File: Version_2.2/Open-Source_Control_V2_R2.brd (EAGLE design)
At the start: 121.9 x 129.5 mm, 344 parts, among them IC10 MCP6002SMT, IC11 MCP6002SMT, IC12 MCP6002SMT, IC14 MCP6002SMT, IC2 ULN2003AD, IC4 74HC165D, IC5 74HC165D, J24 6p-2.54, K1 JS1-24V-F, K2 JS1-24V-F, K3 JS1-24V-F, K4 JS1-24V-F, K5 JS1-24V-F, Q1 MMBT2907, T4 DA2304-AL, U1 OSD3358-512M-ICB, U16 AT97SC3205T-G3M4400B, U2 TPD4S012_DRY_6_P1_M, U27 LAN8710, U28 TCAN1051HV, U29 MAX3483EESA+T, U4 APX811-31UGSOT, U40 ISO3086TDW, U5 TLVH431, U6 SN74LVC2G241_DCU_8, X1 10118194-0001LF, X10 MC4, X11 MC4, X12 MC4, X2 J0011D01BNL, X21 MC10, X24 MSTBA2, X3 MC4, X4 CTI-JTAG, X41 MSTBA3, X5 DM3CS-SF, X6 6p-2.54, X7 TH-2X10, X8 MC4, Y7 7A-25.000MAAE-T

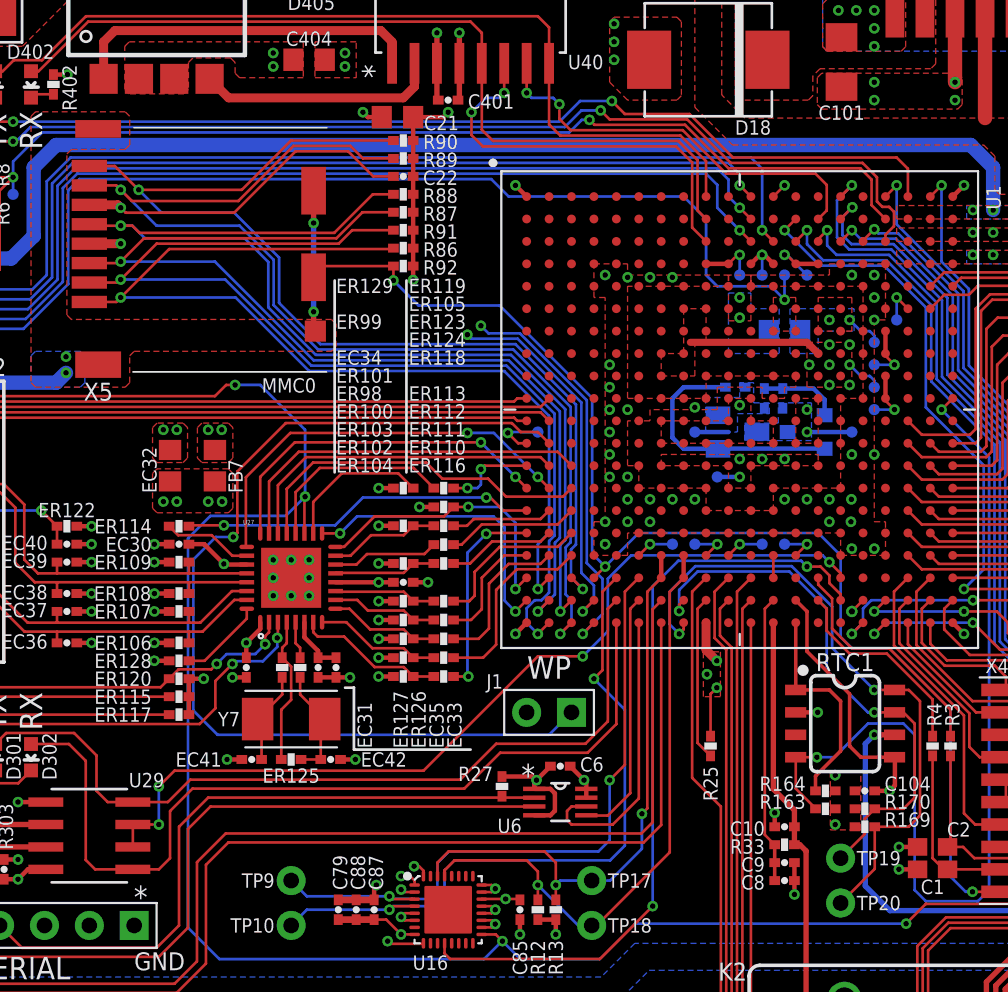
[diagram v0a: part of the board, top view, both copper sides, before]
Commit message: Add files via upload
adding PRU UART option
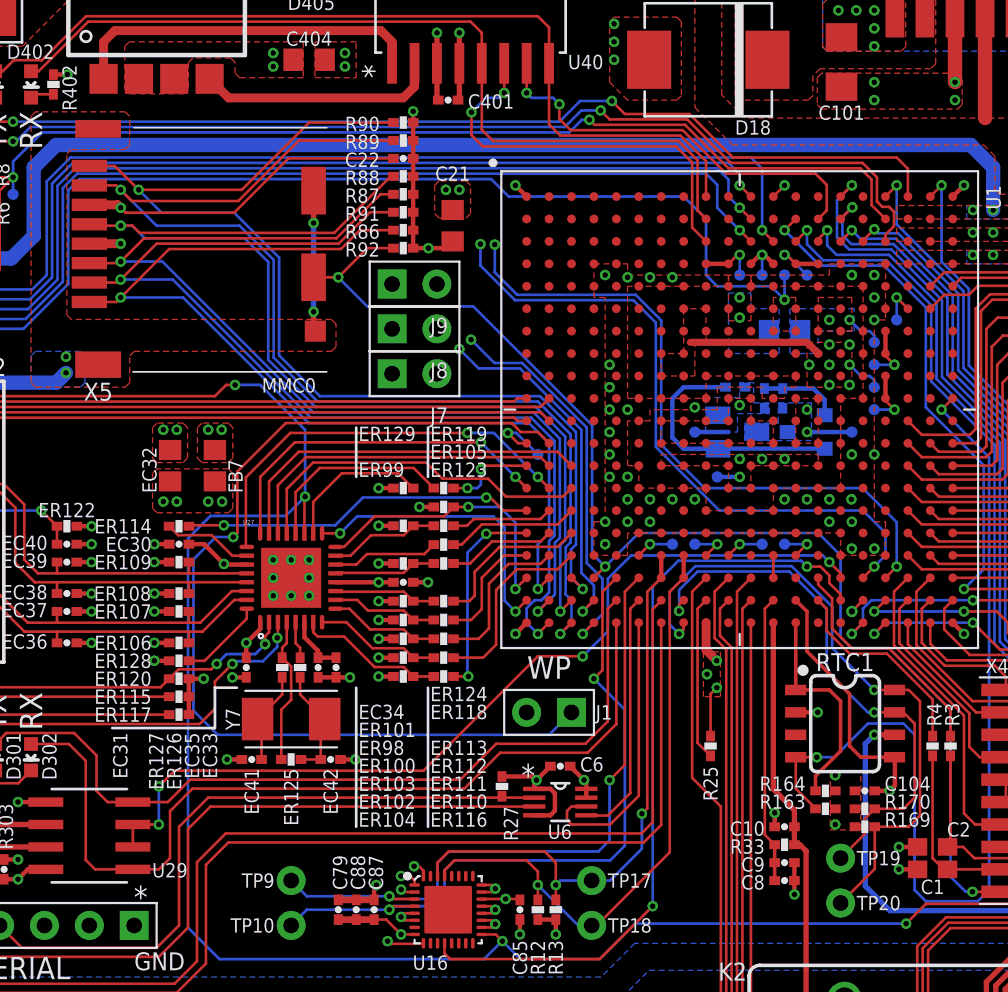
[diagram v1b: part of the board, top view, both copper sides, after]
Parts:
- added J7, J8, J9: (no value), OSD3358-SM-RED Platform:H2-2.54
- moved C21 6.90 mm to (44.7, 100.6), turned to 90 degrees
- moved TP32 1.27 mm to (49.5, 87.6)
- moved C22 1.02 mm to (41.9, 104.4)
- moved R86 1.02 mm to (41.9, 100.3)
- moved R88 1.02 mm to (41.9, 103.4)
- moved R90 1.02 mm to (41.9, 106.4)
- moved R91 1.02 mm to (41.9, 101.3)
- moved R87 1.02 mm to (41.9, 102.4)
- moved R89 1.02 mm to (41.9, 105.4)
- moved R92 1.02 mm to (41.9, 99.3)
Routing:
- net PR1_PRU0_PRU_R30_6: track 0.00 -> 37.7 mm, vias 0 -> 2
- net PR1_PRU0_PRU_R30_7: track 0.00 -> 37.6 mm, vias 0 -> 2
- net GND: track 184.2 -> 182.3 mm, vias 188 -> 189
- net MMC0_CD: track 70.5 -> 72.4 mm
- net MMC0_CLK: track 61.8 -> 63.0 mm
- net MMC0_DAT1: track 62.0 -> 63.2 mm
- net SYS_VDD1_3P3V: track 81.4 -> 80.2 mm
- net PR1_UART0_RXD: track 21.3 -> 20.5 mm
- net PR1_UART0_TXD: track 22.7 -> 22.0 mm
- net MMC0_DAT0: track 65.5 -> 66.2 mm

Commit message: Add files via upload
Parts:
- moved D805 3.81 mm to (109.2, 14.0)
- renumbered J7 to J450, J8 to J45, J9 to J454
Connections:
- new net 485_RXD: D402.1, J45.1, U40.5
- new net 485_TXD: D401.1, J45.2, U40.8
- net CAN_H: now also X8.3; no longer X8.2
- net CAN_L: now also X8.2; no longer X8.1
- net GND: now also X8.1; no longer X8.3
- net GPIO1_16: no longer U40.7
- net GPIO1_28: no longer U40.6
- net PR1_PRU0_PRU_R30_6: now also U40.6
- net PR1_PRU0_PRU_R30_7: now also U40.7
- net PR1_UART0_RXD: now also J450.1
- net PR1_UART0_TXD: now also J450.2
- net UART4_RXD: now also J454.1; no longer D402.1, U40.5
- net UART4_TXD: now also J454.2; no longer D401.1, U40.8
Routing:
- net 485_TXD: track 0.00 -> 58.6 mm
- net 485_RXD: track 0.00 -> 47.7 mm
- net UART4_TXD: track 50.2 -> 17.4 mm, vias 0 -> 1
- net UART4_RXD: track 48.9 -> 19.3 mm, vias 0 -> 1
- net GPIO1_16: track 23.4 -> 0.00 mm, vias 2 -> 0
- net GPIO1_28: track 23.2 -> 0.00 mm, vias 2 -> 0
- net PR1_PRU0_PRU_R30_6: track 37.7 -> 51.0 mm
- net PR1_PRU0_PRU_R30_7: track 37.6 -> 47.9 mm
- net PR1_UART0_RXD: track 20.5 -> 24.8 mm, vias 2 -> 1
- net CAN_H: track 40.7 -> 42.6 mm
- net N$129: track 124.1 -> 122.5 mm
- net CAN_L: track 40.5 -> 42.0 mm
- net PR1_UART0_TXD: track 22.0 -> 23.2 mm
- net USR3: track 64.4 -> 63.8 mm

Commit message: Add files via upload
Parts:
- D19, D31, D32, D33, D34, D35: value LTST-C191KRKT -> LTST-C191KGKT
- D301, D401: value LTST-C191KGKT -> LTST-C191KRKT
- D302, D402: value LTST-C191KFKT -> LTST-C191KGKT
- D801: value LTST-C191KFKT -> LTST-C191KRKT
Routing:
- net PR1_PRU0_PRU_R30_7: track 47.9 -> 48.4 mm
- net GND: vias 189 -> 191

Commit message: Add files via upload
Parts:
- added R215, R225, R235, R245, R255, R265: 100K, OSD3358-SM-RED Platform:R0805
- moved IC14 11.7 mm to (64.8, 14.0)
- moved U$1 9.67 mm to (57.1, 14.0)
- moved U28 2.54 mm to (74.9, 7.11)
- moved C801 2.54 mm to (69.3, 7.11)
- moved J4 1.27 mm to (74.9, 15.2)
- moved J5 1.27 mm to (74.9, 17.8)
- moved J6 1.27 mm to (74.9, 20.3)
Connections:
- net AGND: now also R215.2, R225.2, R235.2, R245.2, R255.2, R265.2; no longer IC14.4
- net AIN1: now also R215.1
- net AIN2: now also R225.1
- net AIN3: now also R235.1
- net AIN4: now also R245.1
- net AIN5: now also R255.1
- net AIN6: now also R265.1
- net GND: now also IC14.4
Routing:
- net 1P8V_REF_1: track 143.7 -> 103.2 mm
- net 1P8V_REF_2: track 69.3 -> 51.6 mm
- net SYS_ADC_1P8V: track 70.3 -> 62.2 mm
- net AIN6: track 84.9 -> 79.3 mm
- net CAN_L: track 42.0 -> 39.5 mm
- net CAN_H: track 42.6 -> 40.0 mm
- net AIN5: track 70.7 -> 72.8 mm
- net EHRPWM1A: track 117.5 -> 115.5 mm
- net EHRPWM2A: track 112.5 -> 110.6 mm
- net EHRPWM2B: track 109.5 -> 107.8 mm
- net SYS_VDD1_3P3V: track 80.4 -> 78.8 mm, vias 40 -> 41
- net AGND: track 168.9 -> 167.3 mm, vias 9 -> 8
- net AIN2: track 48.0 -> 49.2 mm
- net GND: vias 191 -> 193
- added copper zone on layer 1, net 1P8V_REF_1
- added copper zone on layer 1, net 1P8V_REF_2
- added copper zone on layer 15, net AGND
- removed copper zone on layer 2, net AGND

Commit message: Add files via upload
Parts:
- moved R235 0.63 mm to (51.4, 37.5)
- moved R265 0.41 mm to (48.0, 7.49)
- moved R215 0.36 mm to (51.4, 54.5)
- moved R255 0.36 mm to (51.4, 20.4)
- moved R245 0.36 mm to (48.0, 24.5)
- moved R225 0.18 mm to (48.0, 41.5)
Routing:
- net SYS_ADC_1P8V: track 62.2 -> 72.5 mm, vias 0 -> 2
- net AIN2: track 49.2 -> 52.5 mm
- net AIN4: track 64.9 -> 68.2 mm
- net AIN6: track 79.3 -> 82.7 mm
- net AIN3: track 54.6 -> 56.7 mm
- net AIN1: track 38.7 -> 40.7 mm
- net AIN5: track 72.8 -> 74.9 mm
- net GND: vias 193 -> 195
- net AGND: vias 8 -> 10
- added copper zone on layer 15, net 24VAC_IN
- added copper zone on layer 2, net AGND
- removed copper zone on layer 1, net 24VAC_IN
- removed copper zone on layer 15, net AGND

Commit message: Add files via upload
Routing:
- net AGND: track 167.3 -> 7.92 mm, vias 10 -> 38

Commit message: Add files via upload
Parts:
- moved U$1 1.42 mm to (56.5, 12.7)
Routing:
- net AGND: vias 38 -> 58
- net 24VDC_AUX: vias 7 -> 9
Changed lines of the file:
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@@
 <text x="10.16" y="63.119" size="1.27" layer="21" ratio="12" align="center-left">+</text>
 <text x="10.287" y="70.739" size="1.27" layer="21" ratio="12" align="center-left">GND</text>
+<text x="10.287" y="59.309" size="1.27" layer="21" ratio="12" align="center-left">24</text>
 </plain>
 <attributes>
@@
 <element name="X6" library="OSD3358-BSP Ref Design" package="H6-2.54" value="6p-2.54" x="20.32" y="60.96" smashed="yes" rot="R270">
 <attribute name="MPN" value="P125-1106A1BS116A1" x="20.32" y="60.96" size="1.778" layer="27" rot="R270" display="off"/>
+<attribute name="NAME" x="28.067" y="62.357" size="1.016" layer="25" align="top-left"/>
 <attribute name="NAME" x="17.78" y="60.325" size="0.635" layer="33" ratio="10"/>
-<attribute name="NAME" x="12.573" y="59.563" size="1.016" layer="25" align="top-left"/>
 <attribute name="VALUE" x="20.32" y="60.452" size="0.254" layer="27" align="top-center"/>
 </element>
@@
 <attribute name="VALUE" x="97.5106" y="5.08" size="0.254" layer="27" rot="R90" align="top-center"/>
 </element>
-<element name="U$1" library="oshw" package="OSHW_8MM" value="" x="57.15" y="13.97" smashed="yes"/>
+<element name="U$1" library="oshw" package="OSHW_8MM" value="" x="56.515" y="12.7" smashed="yes"/>
 <element name="T4" library="OSD3358-SM-RED Platform" package="DA230X-AL" value="DA2304-AL" x="27.94" y="114.3" smashed="yes" rot="R90">
 <attribute name="NAME" x="32.512" y="118.6434" size="1.016" layer="25"/>
@@
 <element name="J24" library="OSD3358-SM-RED Platform" package="H3-2.54" value="6p-2.54" x="98.425" y="105.41" smashed="yes">
 <attribute name="MPN" value="P125-1106A1BS116A1" x="98.425" y="105.41" size="1.778" layer="27" display="off"/>
-<attribute name="NAME" x="98.425" y="101.3714" size="0.889" layer="25" ratio="10" align="top-center"/>
 <attribute name="NAME" x="99.06" y="102.87" size="0.635" layer="33" ratio="10" rot="R90"/>
+<attribute name="NAME" x="98.425" y="101.3714" size="0.889" layer="25" ratio="10" align="top-center"/>
 <attribute name="VALUE" x="98.425" y="104.14" size="0.254" layer="27" align="center"/>
 </element>
@@
 </element>
 <element name="R265" library="OSD3358-SM-RED Platform" package="R0805" value="100K" x="48.006" y="7.493" smashed="yes" rot="R180">
-<attribute name="NAME" x="50.038" y="7.493" size="0.8128" layer="25" align="center-left"/>
+<attribute name="NAME" x="48.006" y="8.5344" size="0.8128" layer="25" align="bottom-center"/>
 <attribute name="VALUE" x="48.006" y="6.7564" size="0.254" layer="27" align="top-center"/>
 </element>
@@
 <via x="35.0012" y="13.208" extent="1-16" drill="0.3048"/>
 <via x="35.0012" y="12.446" extent="1-16" drill="0.3048"/>
+<via x="57.15" y="55.88" extent="1-16" drill="0.3048"/>
+<via x="57.15" y="51.816" extent="1-16" drill="0.3048"/>
+<via x="57.15" y="48.006" extent="1-16" drill="0.3048"/>
+<via x="57.15" y="44.196" extent="1-16" drill="0.3048"/>
+<via x="57.15" y="34.798" extent="1-16" drill="0.3048"/>
+<via x="6.35" y="55.88" extent="1-16" drill="0.3048"/>
+<via x="6.35" y="51.816" extent="1-16" drill="0.3048"/>
+<via x="6.35" y="48.006" extent="1-16" drill="0.3048"/>
+<via x="6.35" y="44.196" extent="1-16" drill="0.3048"/>
+<via x="6.35" y="39.497" extent="1-16" drill="0.3048"/>
+<via x="6.35" y="34.798" extent="1-16" drill="0.3048"/>
+<via x="6.35" y="30.988" extent="1-16" drill="0.3048"/>
+<via x="6.35" y="27.178" extent="1-16" drill="0.3048"/>
+<via x="6.35" y="22.479" extent="1-16" drill="0.3048"/>
+<via x="6.35" y="17.78" extent="1-16" drill="0.3048"/>
+<via x="6.35" y="13.97" extent="1-16" drill="0.3048"/>
+<via x="6.35" y="10.16" extent="1-16" drill="0.3048"/>
+<via x="6.35" y="6.35" extent="1-16" drill="0.3048"/>
+<via x="57.15" y="39.497" extent="1-16" drill="0.3048"/>
+<via x="57.15" y="6.35" extent="1-16" drill="0.3048"/>
 </signal>
 <signal name="B_UART0_RX">
@@
 <vertex x="10.3632" y="61.214"/>
 <vertex x="10.9982" y="60.579"/>
-<vertex x="10.9982" y="57.15"/>
-<vertex x="10.3632" y="56.515"/>
-<vertex x="0.762" y="56.515"/>
-<vertex x="0.127" y="57.15"/>
+<vertex x="10.9982" y="57.785"/>
+<vertex x="10.3632" y="57.15"/>
+<vertex x="0.762" y="57.15"/>
+<vertex x="0.127" y="57.785"/>
 <vertex x="0.127" y="129.413"/>
 <vertex x="105.918" y="129.413"/>
@@
 </polygon>
 <contactref element="X8" pad="4"/>
+<via x="101.6" y="62.992" extent="1-16" drill="0.3048"/>
+<via x="102.616" y="62.992" extent="1-16" drill="0.3048"/>
 </signal>
 <signal name="N$93">

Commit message: Add files via upload
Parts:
- added J7: (no value), OSD3358-SM-RED Platform:H2-2.54
- moved U$2 1.27 mm to (61.0, 0.64)
- moved U$1 0.63 mm to (57.1, 12.7)
- turned J1 to 90 degrees
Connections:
- net AGND: now also J7.1
- net GND: now also J7.2
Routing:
- net EEPROM_WP: track 56.9 -> 54.4 mm
- net CAN1_TXD: track 240.3 -> 238.2 mm
- net CAN1_RXD: track 226.8 -> 226.1 mm
- net AGND: vias 58 -> 61
- added copper zone on layer 16, net AGND
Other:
- board text added: "AGND"
